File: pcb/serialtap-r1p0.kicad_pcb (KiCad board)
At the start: 4 copper layers, 40 x 25 mm, 0 parts

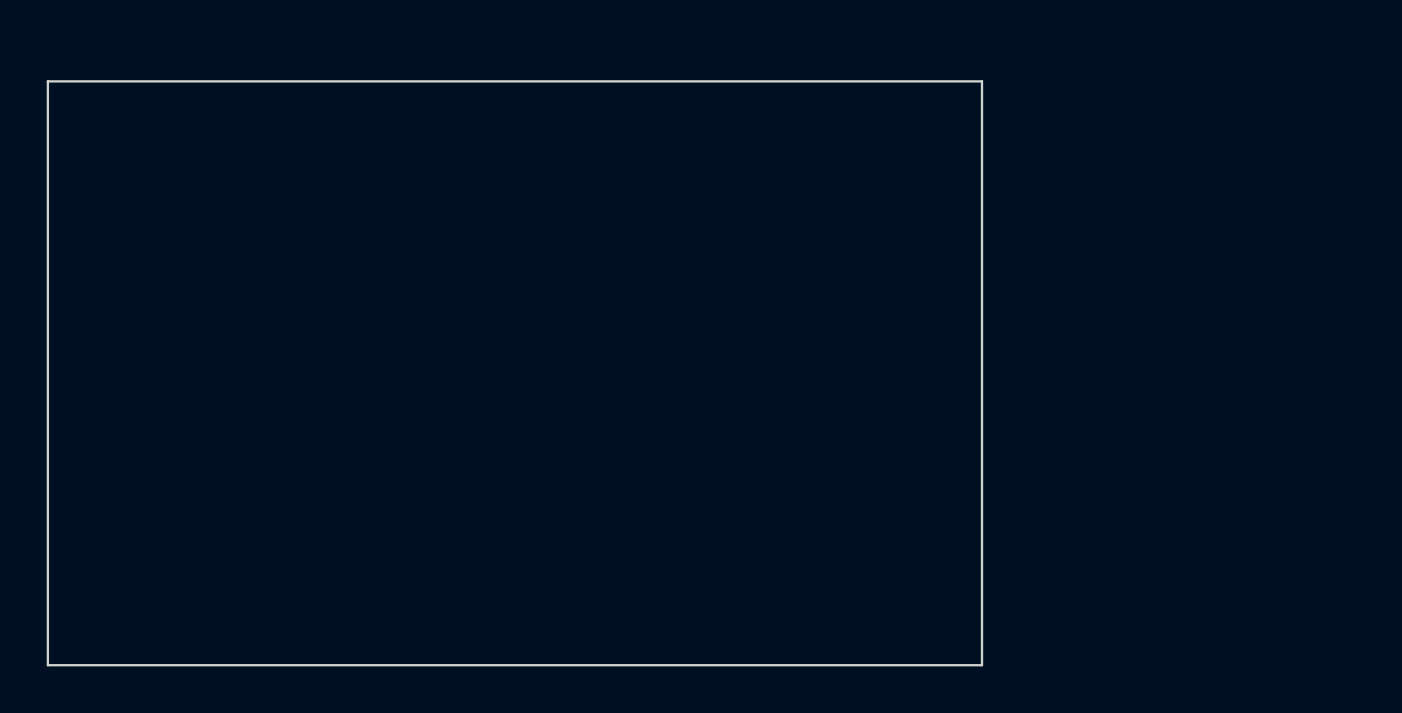
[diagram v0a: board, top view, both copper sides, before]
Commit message: pcb: outline 22 x 54 mm to drop into the OEM Haier board's place
More area than the 40 x 25 it replaces (1188 vs 1000 mm2) and a longer
axis to zone along, which helps the constraint that matters most -
maximum distance between the buck's switch node and the module antenna.

One rule had to change. layout-rules.md put both connectors on the same
short edge; they do not fit across 22 mm. A 5-position XA header is
~14.6 mm and a USB-C receptacle ~8.9 mm, needing ~26 mm with edge
clearance. The JST keeps the short edge because it carries the permanent
harness and wants a clean cable exit; USB-C moves to the adjacent long
edge, which costs nothing because it is bench-only and unused after
first flash (ADR 0002). Both still land at the same end, so the two 5 V
sources still meet at the ideal-diode OR without crossing the board.

DRC clean.

Co-Authored-By: Claude Opus 5 <noreply@anthropic.com>
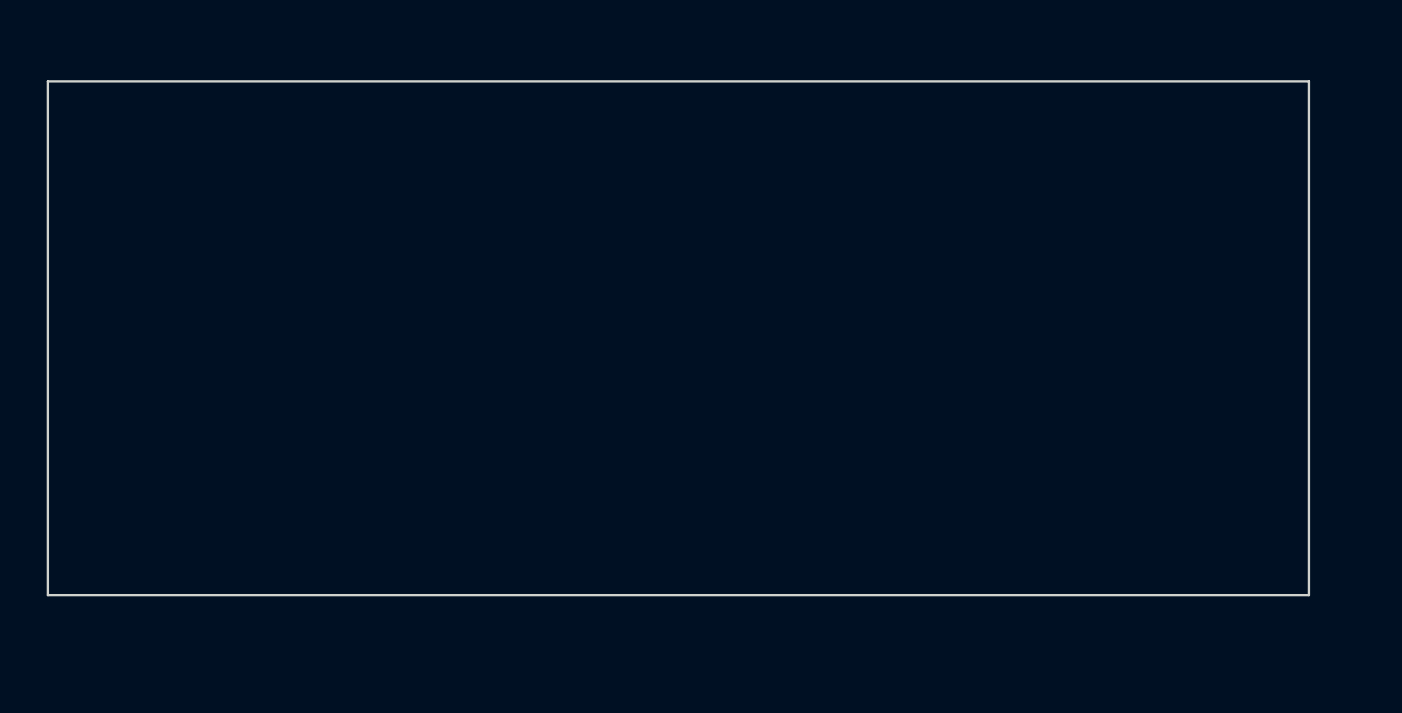
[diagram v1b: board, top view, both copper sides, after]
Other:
- board size 40 x 25 mm -> 54 x 22 mm
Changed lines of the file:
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@@
 	(gr_rect
 		(start 100 100)
-		(end 140 125)
+		(end 154 122)
 		(stroke
 			(width 0.1)

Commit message: Place and route r1p0, and fix three library defects on the way
Netlist imported into the PCB, all 43 footprints placed inside the
22 x 54 mm outline with the module's antenna keepout on-board (the slot
is the whole envelope, so no overhang), and all 138 connections routed:
signals and parts on L1, solid GND on L2, a V5 pour plus 3V3 traces on
L3, GND on L4 with the ten test points as bare pads. DRC is clean apart
from silkscreen warnings; zero unconnected, schematic parity zero.

The TVS channel assignment was swapped in the schematic so the USB pair
enters pins 1/2 and the UART pins 4/5 - the only order that routes the
pair to the array without a crossing. Net-class patterns (Power, USB)
now actually apply to nets; they were defined but unassigned.

Library defects found by the first DRC and render, fixed in lib/ and on
the board: the LM66200 footprint had no courtyard, the TPS62162 thermal
vias were drilled at 0.2 mm against the 0.25 mm fab minimum, and the JST
XA 3D model sat 10 mm off its pads.

Compromises still to record in the layout rules: the UART from the JST
runs on L3 with L1 hops (TVS 9 mm from the JST, 3 mm from the USB-C),
one TVS stub uses L3, CC2 passes under the USB-C body, and L4 carries
test-point pads. Fiducials, silkscreen tidy and review gate 2 remain.

Co-Authored-By: Claude Fable 5.1 <noreply@anthropic.com>
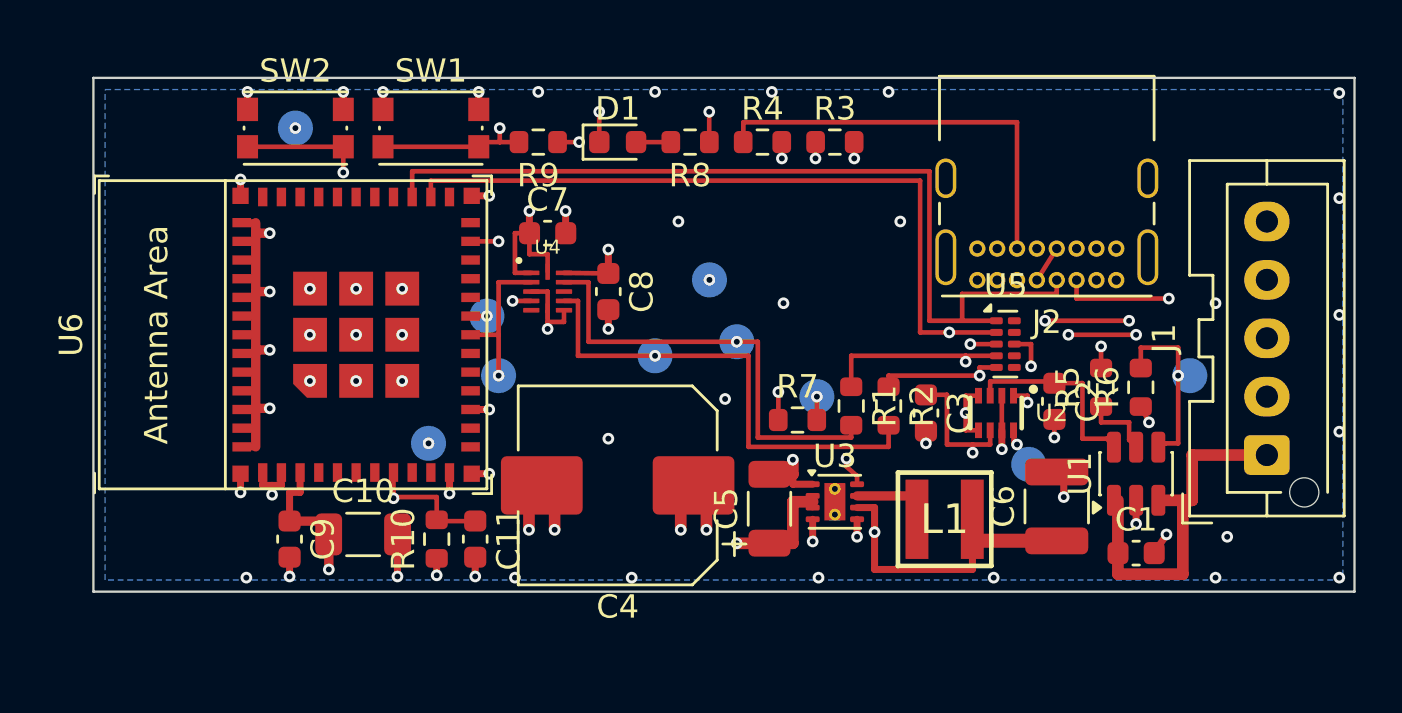
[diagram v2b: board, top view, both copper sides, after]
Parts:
- added C1: 0.1u, serialtap:C_0603_1608Metric, F.Cu at (146.6, 120.2)
- added C10: 10u, serialtap:C_1206_3216Metric, F.Cu at (113.5, 119.4)
- added C11: 1u, serialtap:C_0603_1608Metric, F.Cu at (118.3, 119.6)
- added C2: 1u, serialtap:C_0603_1608Metric, F.Cu at (143.1, 113.7)
- added C3: 1u, serialtap:C_0603_1608Metric, F.Cu at (137.6, 114.2)
- added C4: PCL1A471MCL1GS, serialtap:CP_Elec_8x10, F.Cu at (124.4, 117.3)
- added C5: 10u, serialtap:C_1206_3216Metric, F.Cu at (130.9, 118.3)
- added C6: 22u, serialtap:C_1210_3225Metric, F.Cu at (143.2, 118.2)
- added C7: 0.1u, serialtap:C_0603_1608Metric, F.Cu at (121.4, 106.5)
- added C8: 0.1u, serialtap:C_0603_1608Metric, F.Cu at (124.0, 109.0)
- added C9: 0.1u, serialtap:C_0603_1608Metric, F.Cu at (110.3, 119.6)
- added D1: LED, serialtap:LED_0603_1608Metric, F.Cu at (124.4, 102.6)
- added J1: B05B-XASK-1-A, serialtap:JST_XA_B05B-XASK-1-A_1x05_P2.50mm_Vertical, F.Cu at (152.2, 116.0)
- added J2: USB4085-GF-A, serialtap:USB_C_Receptacle_GCT_USB4085, F.Cu at (145.8, 108.5)
- added L1: XGL4020-222MEC, serialtap:L_Coilcraft_XGL4020_4.0x4.0mm, F.Cu at (138.4, 118.8)
- added R1: 330, serialtap:R_0603_1608Metric, F.Cu at (134.4, 113.9)
- added R10: 10k, serialtap:R_0603_1608Metric, F.Cu at (116.7, 119.6)
- added R2: 330, serialtap:R_0603_1608Metric, F.Cu at (136.0, 113.9)
- added R3: 5.1k, serialtap:R_0603_1608Metric, F.Cu at (133.7, 102.6)
- added R4: 5.1k, serialtap:R_0603_1608Metric, F.Cu at (130.6, 102.6)
- added R5: 66.5k, serialtap:R_0603_1608Metric, F.Cu at (145.1, 113.1)
- added R6: 100k, serialtap:R_0603_1608Metric, F.Cu at (146.8, 113.1)
- added R7: 100k, serialtap:R_0603_1608Metric, F.Cu at (132.1, 114.5)
- added R8: 5.1k, serialtap:R_0603_1608Metric, F.Cu at (127.5, 102.6)
- added R9: 2.2k, serialtap:R_0603_1608Metric, F.Cu at (121.0, 102.6)
- added SW1: SW_Push, serialtap:SW_Push_1P1T_NO_CK_KMR2, F.Cu at (116.4, 102.0)
- added SW2: SW_Push, serialtap:SW_Push_1P1T_NO_CK_KMR2, F.Cu at (110.6, 102.0)
- added TP1: TestPoint, serialtap:TestPoint_Pad_D1.5mm, B.Cu at (128.3, 108.5)
- added TP10: TestPoint, serialtap:TestPoint_Pad_D1.5mm, B.Cu at (142.0, 116.4)
- added TP2: TestPoint, serialtap:TestPoint_Pad_D1.5mm, B.Cu at (116.3, 115.5)
- added TP3: TestPoint, serialtap:TestPoint_Pad_D1.5mm, B.Cu at (110.6, 102.0)
- added TP4: TestPoint, serialtap:TestPoint_Pad_D1.5mm, B.Cu at (129.5, 111.2)
- added TP5: TestPoint, serialtap:TestPoint_Pad_D1.5mm, B.Cu at (126.0, 111.8)
- added TP6: TestPoint, serialtap:TestPoint_Pad_D1.5mm, B.Cu at (119.3, 112.6)
- added TP7: TestPoint, serialtap:TestPoint_Pad_D1.5mm, B.Cu at (118.8, 110.0)
- added TP8: TestPoint, serialtap:TestPoint_Pad_D1.5mm, B.Cu at (148.9, 112.6)
- added TP9: TestPoint, serialtap:TestPoint_Pad_D1.5mm, B.Cu at (132.9, 113.5)
- added U1: TPS2553DBV, serialtap:SOT-23-6, F.Cu at (146.6, 116.8)
- added U2: LM66200DRL, serialtap:TI_DRL0008A_SOT-5X3-8_2.1x1.6mm_P0.5mm, F.Cu at (140.6, 114.2)
- added U3: TPS62162DSG, serialtap:Texas_DSG0008A_WSON-8-1EP_2x2mm_P0.5mm_EP0.9x1.6mm_ThermalVias, F.Cu at (133.7, 118.0)
- added U4: TXU0204RUT, serialtap:TI_RUT0012A_UQFN-12_2.0x1.7mm_P0.4mm, F.Cu at (121.4, 109.0)
- added U5: TPD4E05U06DQA, serialtap:USON-10_2.5x1.0mm_P0.5mm, F.Cu at (141.0, 111.2)
- added U6: ESP32-C3-MINI-1, serialtap:ESP32-C3-MINI-1, F.Cu at (110.5, 110.8)
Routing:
- net V3V3: track 0.00 -> 84.2 mm, vias 0 -> 7
- net GND: track 0.00 -> 57.8 mm, vias 0 -> 71
- net /USB_DM: track 0.00 -> 42.2 mm, vias 0 -> 1
- net /USB_DP: track 0.00 -> 39.9 mm
- net V5: track 0.00 -> 36.8 mm, vias 0 -> 8
- net USB_VBUS: track 0.00 -> 31.5 mm, vias 0 -> 1
- net Net-(J2-CC1): track 0.00 -> 28.1 mm, vias 0 -> 2
- net /PORT_TX: track 0.00 -> 26.4 mm, vias 0 -> 3
- net /C3_EN: track 0.00 -> 25.9 mm, vias 0 -> 2
- net /RX_BUF: track 0.00 -> 21.1 mm, vias 0 -> 1
- net /TX_BUF: track 0.00 -> 19.5 mm, vias 0 -> 1
- net /PORT_RX: track 0.00 -> 19.1 mm, vias 0 -> 3
- net Net-(J2-CC2): track 0.00 -> 18.0 mm
- net PORT_5V: track 0.00 -> 15.8 mm
- net /BOOT: track 0.00 -> 12.8 mm, vias 0 -> 2
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- added copper zone on B.Cu, net GND
- added copper zone on In1.Cu, net GND
- added copper zone on In2.Cu, net V5

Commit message: Clear silkscreen DRC, add fiducials, and record the layout exceptions
DRC is now clean: 0 violations, 0 unconnected, 0 schematic parity.

Silkscreen: text minimums aligned to PCBWay's published capabilities
(0.8 mm high, 0.15 mm stroke; the stroke rule was 0.12 mm, looser than
the fab). U2 and U4 references resized; U4's small text came from the
TXU0204 footprint in lib/, fixed at source. Silk tidied on the board,
and the two footprints trimmed to do it (ESP32-C3-MINI-1, USB4085 -
silkscreen only, pads and keepouts unchanged) written back to lib/ so
the library and board agree.

Three fiducials (serialtap:Fiducial_1mm_Mask2mm, KiCad stock copied
in), board-only and excluded from BOM and placement. They sit in the
right two-thirds of the board: the only free L1 space at the left end
is beside the antenna.

layout-rules.md gains a "Recorded exceptions" section: ESD array
placement relative to J1 (accepted), UART on L3, a TVS stub on L3, CC2
under the grounded USB-C shell, test pads on L4, fiducial spread and
the footprint trims. The VBUS TVS is marked decided-not-fitted where
the gate-1 table still read "open", and board retention is closed:
the board keeps the OEM outline and sits in its slot.

KiCad lock files are now ignored (~*.lck); one had been committed.

Co-Authored-By: Claude Opus 5 <noreply@anthropic.com>
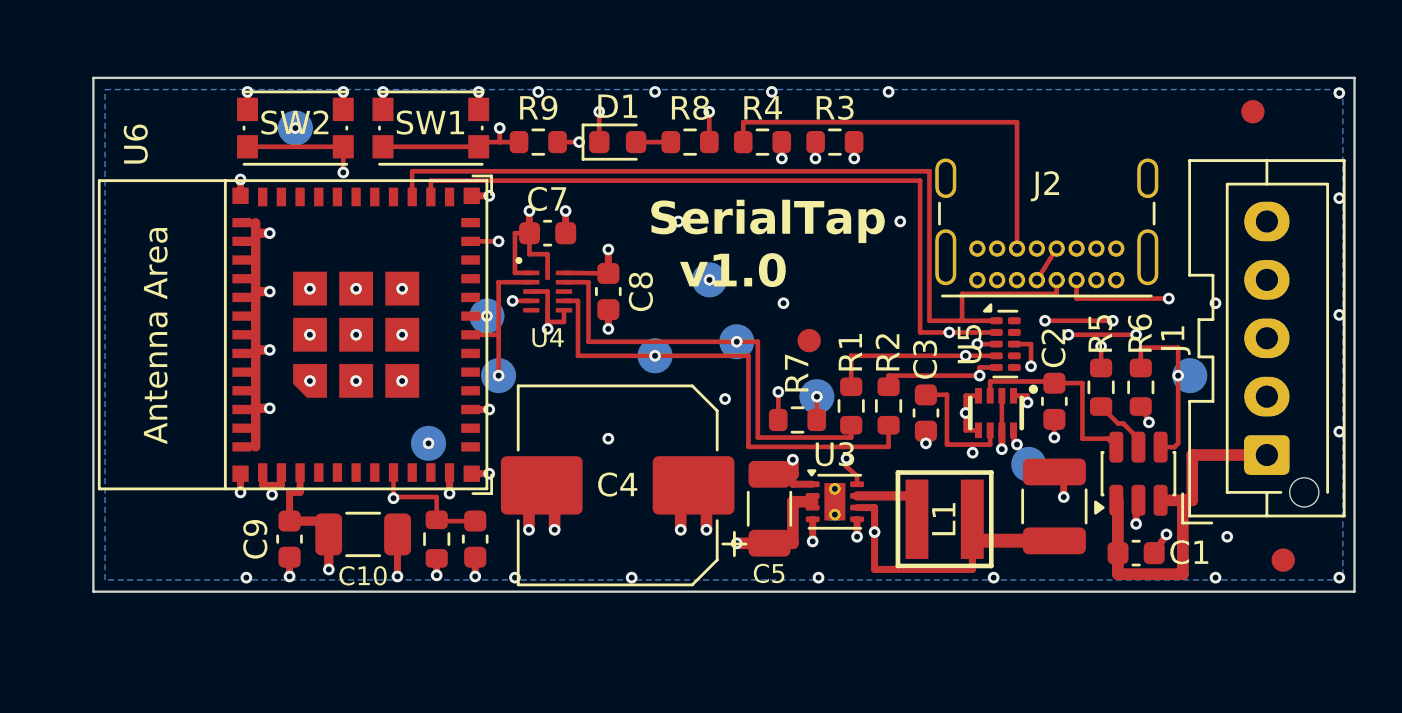
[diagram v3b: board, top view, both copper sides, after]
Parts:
- added FID1: Fiducial_1mm_Mask2mm, serialtap:Fiducial_1mm_Mask2mm, F.Cu at (151.6, 101.3)
- added FID2: Fiducial_1mm_Mask2mm, serialtap:Fiducial_1mm_Mask2mm, F.Cu at (152.9, 120.5)
- added FID3: Fiducial_1mm_Mask2mm, serialtap:Fiducial_1mm_Mask2mm, F.Cu at (132.6, 111.1)
- moved C6 0.10 mm to (143.1, 118.2)
- moved U1 0.10 mm to (146.7, 116.8)
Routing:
- net /PORT_TX: track 26.4 -> 24.9 mm
- net Net-(U1-ILIM): track 3.06 -> 2.53 mm
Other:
- board text added: "SerialTap v1.0"
- board text added: "by: Timothy Findlay 2026"
